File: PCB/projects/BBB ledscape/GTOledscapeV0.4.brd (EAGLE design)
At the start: 100 x 80 mm, 16 parts

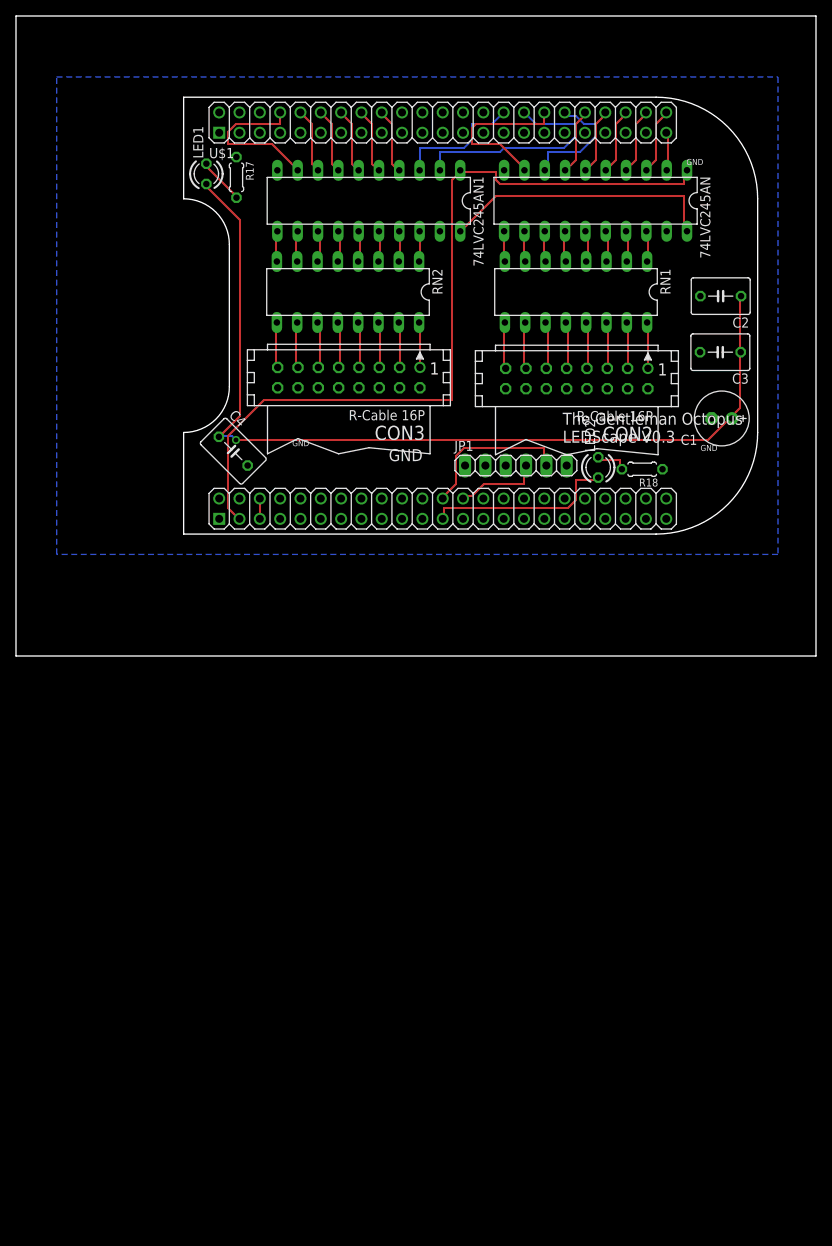
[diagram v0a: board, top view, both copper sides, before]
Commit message: PCB updated to use the 74AHCT245 chip instead of the other level shifter. Should work better for going from 3v3 to 5v
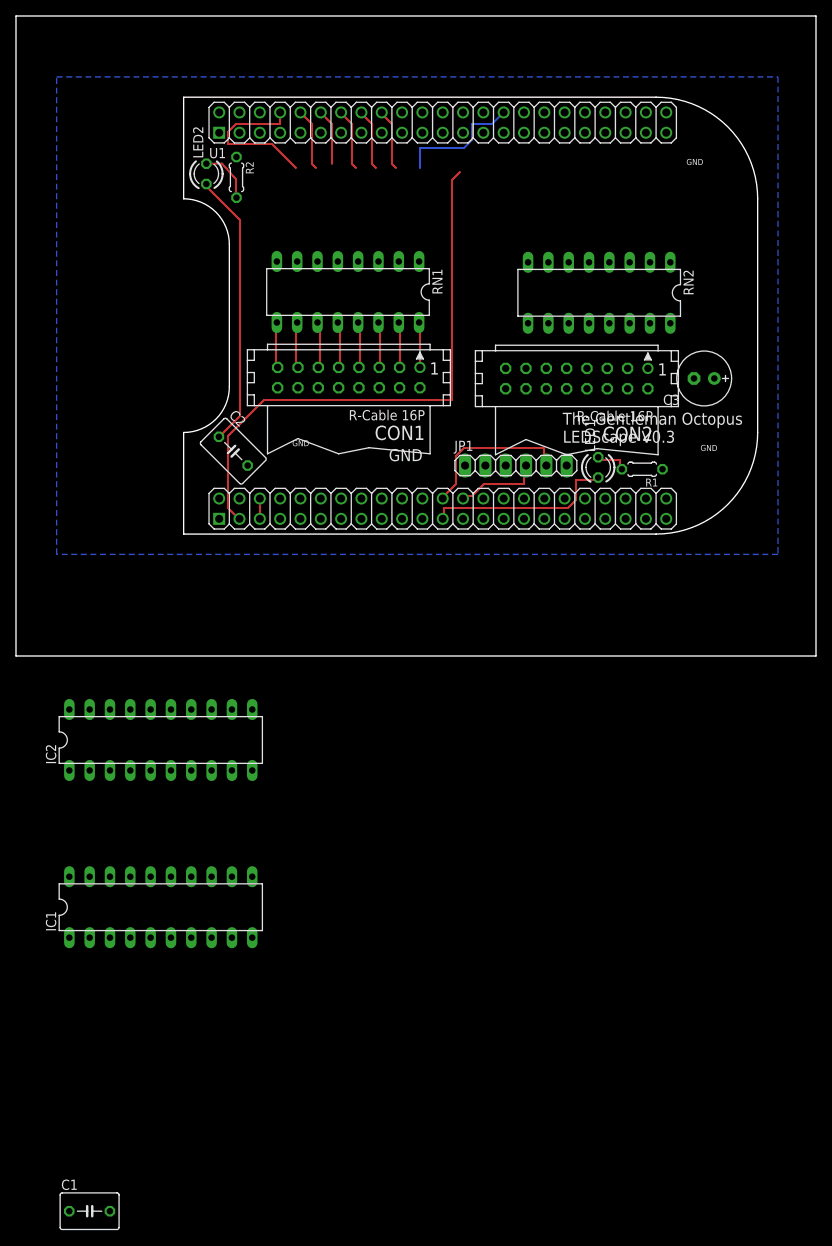
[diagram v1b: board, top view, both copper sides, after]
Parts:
- removed 74LVC245AN, 74LVC245AN1: (no value), tgo_custom:DIL20
- removed C4: (no value), rcl:C050-045X075
- added IC1, IC2: 74HC245N, 74xx-eu:DIL20
- C1: device rcl:E2,5-7 -> rcl:C050-045X075
- C3: device rcl:C050-045X075 -> rcl:E2,5-7
- moved C1 126.7 mm to (9.20, -69.4), turned to 0 degrees
- moved C2 63.9 mm to (27.2, 25.6), turned to 315 degrees
- moved LED1 61.2 mm to (72.8, 23.6)
- moved LED2 61.2 mm to (23.8, 60.3)
- moved RN2 31.4 mm to (72.9, 45.4)
- moved RN1 28.5 mm to (41.5, 45.5)
- moved C3 3.86 mm to (86.0, 34.7)
- renumbered CON3 to CON1, R17 to R2, R18 to R1, U$1 to U1
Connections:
- removed net N$21: 74LVC245AN1.18, RN2.1
- removed net N$22: 74LVC245AN1.17, RN2.2
- removed net N$23: 74LVC245AN1.16, RN2.3
- removed net N$24: 74LVC245AN1.15, RN2.4
- removed net N$25: 74LVC245AN1.14, RN2.5
- removed net N$26: 74LVC245AN1.13, RN2.6
- removed net N$27: 74LVC245AN1.12, RN2.7
- removed net N$28: 74LVC245AN1.11, RN2.8
- removed net SYS_5V: U1.53
- removed net VDD_V3V: 74LVC245AN.20, 74LVC245AN1.20
- new net N$10: IC1.17, RN1.2
- new net N$11: IC1.16, RN1.3
- new net N$12: IC1.15, RN1.4
- new net N$13: IC1.14, RN1.5
- new net N$14: IC1.13, RN1.6
- new net N$29: IC1.12, RN1.7
- new net N$30: IC1.11, RN1.8
- new net N$7: IC1.18, RN1.1
- net +5V: now also C1.1, C3.+, IC1.1, IC1.20, IC2.1, IC2.20, LED2.A, U1.53, U1.54; no longer C1.+, C3.1, C4.1, LED1.A
- net CH00: now also IC1.2; no longer 74LVC245AN1.2
- net CH00_OP: now also RN1.16; no longer RN2.16
- net CH01: now also IC1.3; no longer 74LVC245AN1.3
- net CH01_OP: now also RN1.15; no longer RN2.15
- net CH02: now also IC1.4; no longer 74LVC245AN1.4
- net CH02_OP: now also RN1.14; no longer RN2.14
- net CH03: now also IC1.5; no longer 74LVC245AN1.5
- net CH03_OP: now also RN1.13; no longer RN2.13
- net CH04: now also IC1.6; no longer 74LVC245AN1.6
- net CH04_OP: now also RN1.12; no longer RN2.12
- net CH05: now also IC1.7; no longer 74LVC245AN1.7
- net CH05_OP: now also RN1.11; no longer RN2.11
- net CH06: now also IC1.8; no longer 74LVC245AN1.8
- net CH06_OP: now also RN1.10; no longer RN2.10
- net CH07: now also IC1.9; no longer 74LVC245AN1.9
- net CH07_OP: now also RN1.9; no longer RN2.9
- net CH08: now also IC2.2; no longer 74LVC245AN.2
- net CH08_OP: now also RN2.16; no longer RN1.16
- net CH09: now also IC2.3; no longer 74LVC245AN.3
- net CH09_OP: now also RN2.15; no longer RN1.15
- net CH10: now also IC2.4; no longer 74LVC245AN.4
- net CH10_OP: now also RN2.14; no longer RN1.14
- net CH11: now also IC2.5; no longer 74LVC245AN.5
- net CH11_OP: now also RN2.13; no longer RN1.13
- net CH12: now also IC2.6; no longer 74LVC245AN.6
- net CH12_OP: now also RN2.12; no longer RN1.12
- net CH13: now also IC2.7; no longer 74LVC245AN.7
- net CH13_OP: now also RN2.11; no longer RN1.11
- net CH14: now also IC2.8; no longer 74LVC245AN.8
- net CH14_OP: now also RN2.10; no longer RN1.10
- net CH15: now also IC2.9; no longer 74LVC245AN.9
- net CH15_OP: now also RN2.9; no longer RN1.9
- net GND: now also C1.2, C3.-, IC1.10, IC1.19, IC2.10, IC2.19; no longer 74LVC245AN.10, 74LVC245AN.19, 74LVC245AN1.10, 74LVC245AN1.19, C1.-, C3.2, C4.2
- net N$1: now also IC2.18, RN2.1; no longer 74LVC245AN.18, RN1.1
- net N$15: now also IC2.16, RN2.3; no longer 74LVC245AN.16, RN1.3
- net N$16: now also IC2.15, RN2.4; no longer 74LVC245AN.15, RN1.4
- net N$17: now also IC2.14, RN2.5; no longer 74LVC245AN.14, RN1.5
- net N$18: now also IC2.13, RN2.6; no longer 74LVC245AN.13, RN1.6
- net N$19: now also IC2.12, RN2.7; no longer 74LVC245AN.12, RN1.7
- net N$2: now also LED2.K; no longer LED1.K
- net N$20: now also IC2.11, RN2.8; no longer 74LVC245AN.11, RN1.8
- net N$3: now also LED1.K; no longer LED2.K
- net N$4: now also LED1.A; no longer LED2.A
- net N$6: now also IC2.17, RN2.2; no longer 74LVC245AN.17, RN1.2
- net VDD_3V3: no longer 74LVC245AN.1, 74LVC245AN1.1
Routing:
- net +5V: track 115.6 -> 34.2 mm, vias 1 -> 0
- net VDD_V3V: track 34.3 -> 0.00 mm
- net VDD_3V3: track 101.1 -> 69.8 mm
- net CH00: track 29.0 -> 0.00 mm
- net CH15: track 20.7 -> 0.00 mm
- net CH14: track 15.3 -> 0.00 mm
- net CH13: track 8.25 -> 0.00 mm
- net CH12: track 8.23 -> 0.00 mm
- net CH11: track 8.22 -> 0.00 mm
- net CH10: track 8.21 -> 0.00 mm
- net CH09: track 8.20 -> 0.00 mm
- net CH13_OP: track 6.08 -> 0.00 mm
- net CH12_OP: track 6.01 -> 0.00 mm
- net CH14_OP: track 6.00 -> 0.00 mm
- net CH11_OP: track 5.94 -> 0.00 mm
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
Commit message: Finished PCB and Ting
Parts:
- moved C1 124.2 mm to (57.2, 45.1), turned to 270 degrees
- moved IC1 92.7 mm to (44.1, 57.6), turned to 180 degrees
- moved IC2 89.0 mm to (75.5, 57.5), turned to 180 degrees
- moved C2 63.5 mm to (87.6, 45.3), turned to 270 degrees
- moved C3 10.4 mm to (87.6, 24.4), turned to 270 degrees
- moved CON2 2.80 mm to (72.9, 34.8)
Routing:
- net +5V: track 34.2 -> 170.1 mm
- net VDD_3V3: track 69.8 -> 0.00 mm
- net CH00: track 0.00 -> 15.1 mm
- net CH07: track 19.6 -> 7.64 mm
- net CH09: track 0.00 -> 8.16 mm
- net CH15: track 0.00 -> 7.78 mm
- net CH13: track 0.00 -> 7.67 mm
- net CH14: track 0.00 -> 7.65 mm
- net CH12: track 0.00 -> 7.57 mm
- net CH10: track 0.00 -> 7.52 mm
- net CH11: track 0.00 -> 7.48 mm
- net CH08: track 0.46 -> 6.69 mm
- net CH15_OP: track 0.00 -> 5.54 mm
- net CH14_OP: track 0.00 -> 5.54 mm
- net CH13_OP: track 0.00 -> 5.54 mm
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- added copper zone on layer 1, net GND
